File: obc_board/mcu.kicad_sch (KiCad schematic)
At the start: 47 parts, among them J4 Micro_SD_Card, U24 TLE9250X, U25 STM32L552ZET6Q, U26 IS66WVH16M8DBLL-100B1LI, Y2 16MHz, Y3 32.768kHz

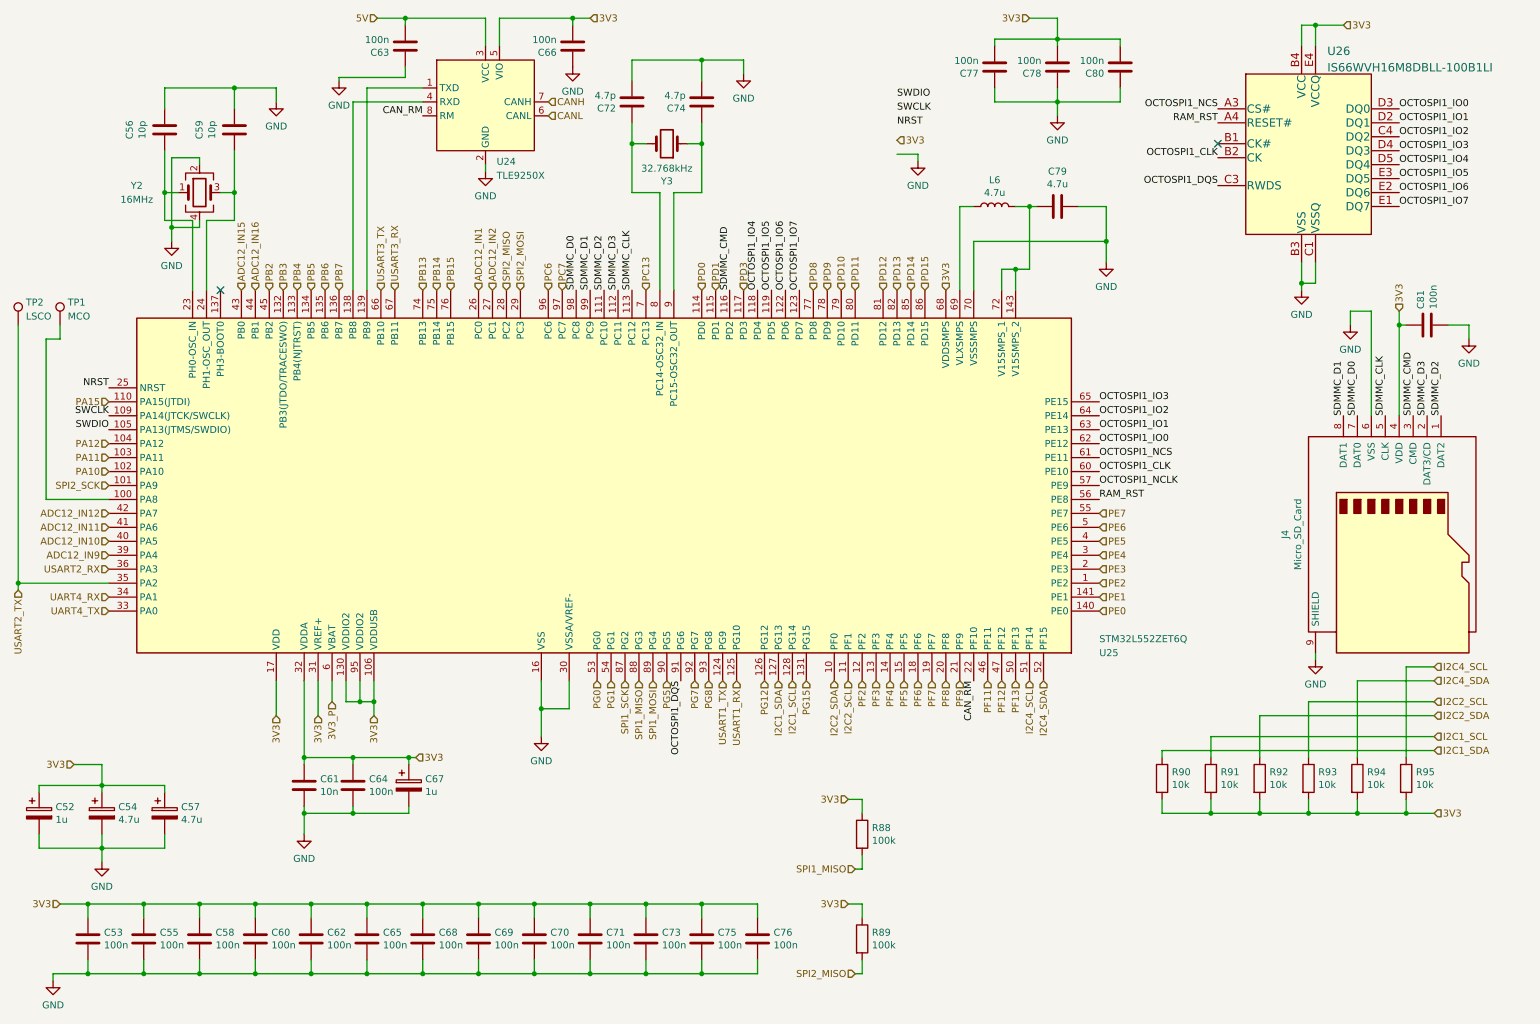
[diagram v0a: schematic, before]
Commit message: remapped magnetorquer pins, routed tespoints
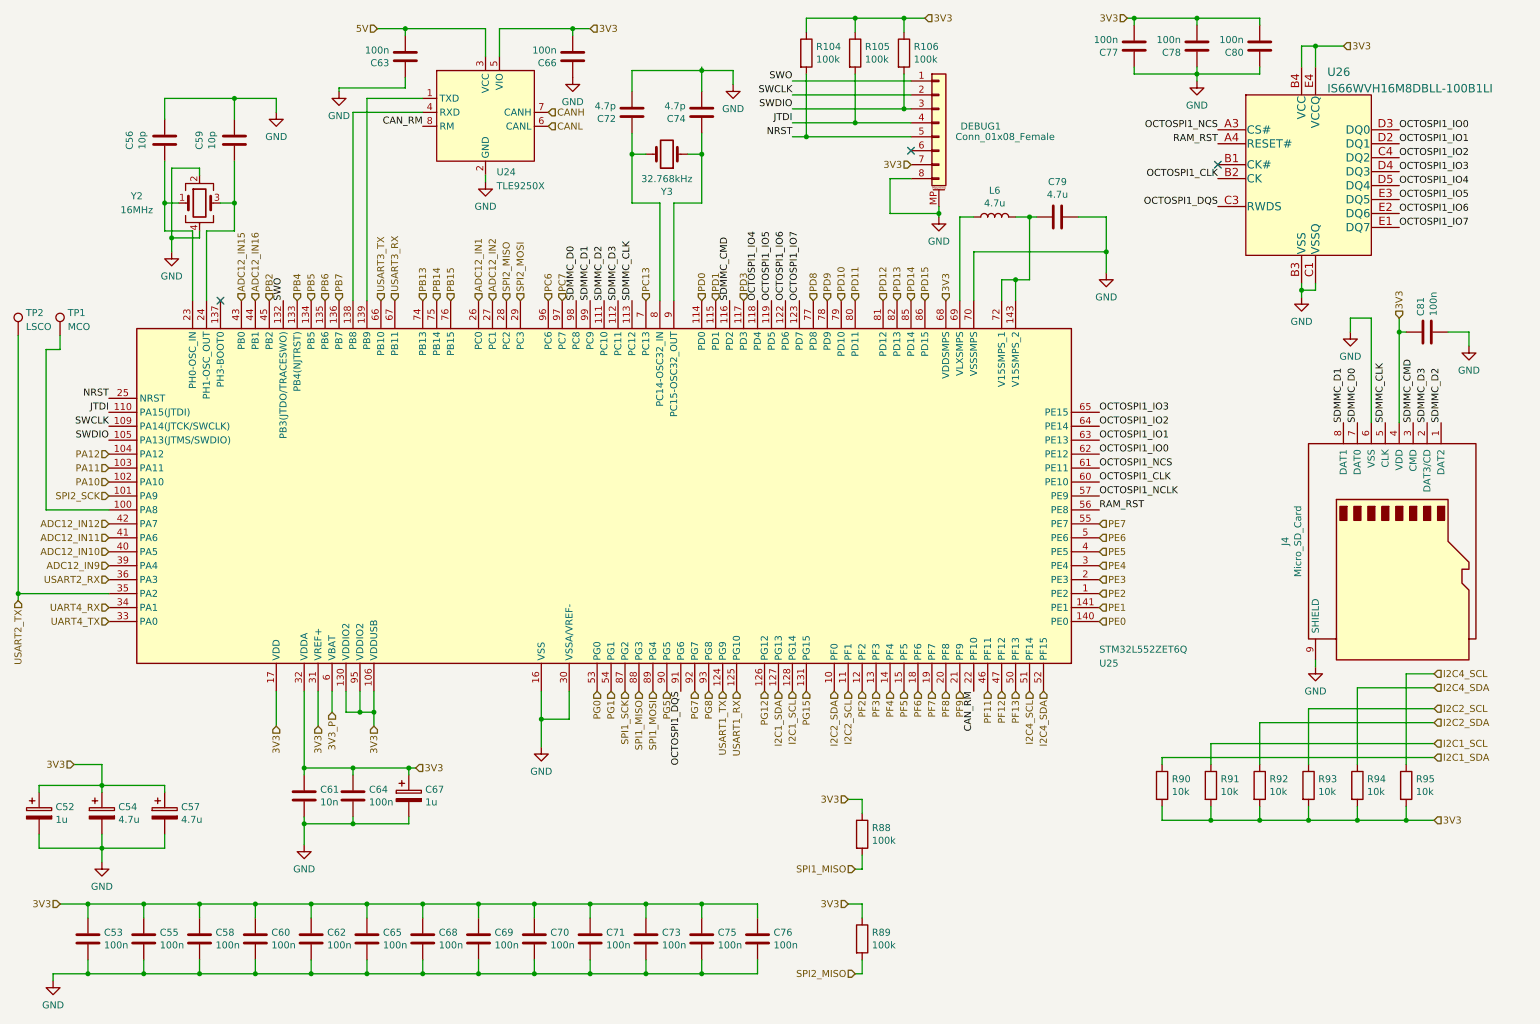
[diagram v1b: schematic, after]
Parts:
- added DEBUG1: Conn_01x08_Female, Connector_Molex:Molex_PicoBlade_53261-0871_1x08-1MP_P1.25mm_Horizontal, symbol Connector_Generic_MountingPin:Conn_01x08_MountingPin
- added R104, R105, R106: 100k, Resistor_SMD:R_0402_1005Metric, symbol Device:R
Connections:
- net GND: now also DEBUG1.8 (Pin_8), DEBUG1.MP (MountPin)
- net NRST: now also DEBUG1.5 (Pin_5), R104.2
- net SWCLK: now also DEBUG1.2 (Pin_2)
- net SWDIO: now also DEBUG1.3 (Pin_3), R106.2
- net VCCQ: now also DEBUG1.7 (Pin_7), R104.1, R105.1, R106.1
- net PA15 renamed JTDI
- net JTDI: now also DEBUG1.4 (Pin_4), R105.2
- net PB3 renamed SWO
- net SWO: now also DEBUG1.1 (Pin_1)
- no-connect marks 2 -> 3
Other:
- moved on the sheet: C56, C59, C61, C63, C64, C66, C67, C72, C74, C77, C78, C79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

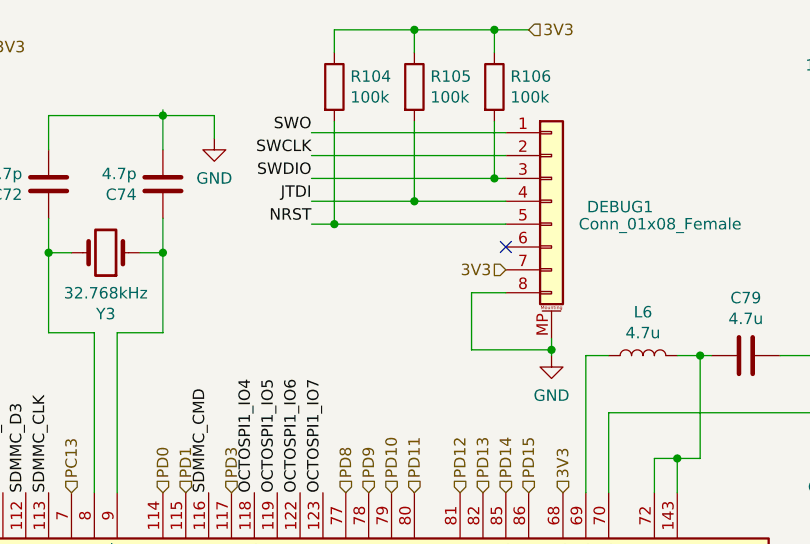
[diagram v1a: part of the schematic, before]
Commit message: routed photodiode circuits, jtag and short circuit prot circuits
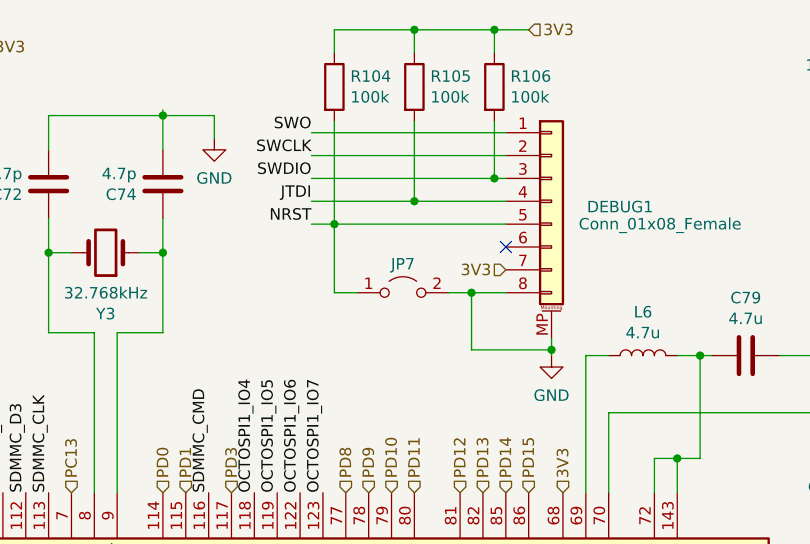
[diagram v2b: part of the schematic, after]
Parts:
- added JP7: Jumper_2_Open, Jumper:SolderJumper-2_P1.3mm_Open_RoundedPad1.0x1.5mm, symbol Jumper:Jumper_2_Open
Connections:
- net GND: now also JP7.2 (B)
- net NRST: now also JP7.1 (A)
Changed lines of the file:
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@@
   (junction (at 166.37 15.24) (diameter 0) (color 0 0 0 0)
+  )
+  (junction (at 172.72 44.45) (diameter 0) (color 0 0 0 0)
   )
   (junction (at 57.15 189.23) (diameter 0) (color 0 0 0 0)
@@
     (stroke (width 0) (type default) (color 0 0 0 0))
   )
+  (wire (pts (xy 170.18 44.45) (xy 172.72 44.45))
+    (stroke (width 0) (type default) (color 0 0 0 0))
+  )
   (wire (pts (xy 78.74 141.605) (xy 78.74 137.795))
     (stroke (width 0) (type default) (color 0 0 0 0))
@@
     (stroke (width 0) (type default) (color 0 0 0 0))
   )
+  (wire (pts (xy 157.48 44.45) (xy 157.48 36.83))
+    (stroke (width 0) (type default) (color 0 0 0 0))
+  )
   (wire (pts (xy 17.78 154.94) (xy 29.21 154.94))
     (stroke (width 0) (type default) (color 0 0 0 0))
@@
   )
   (wire (pts (xy 114.935 17.145) (xy 114.935 18.415))
+    (stroke (width 0) (type default) (color 0 0 0 0))
+  )
+  (wire (pts (xy 160.02 44.45) (xy 157.48 44.45))
     (stroke (width 0) (type default) (color 0 0 0 0))
   )
@@
     (pin "1")
   )
+  (symbol (lib_id "Jumper:Jumper_2_Open") (at 165.1 44.45 0) (unit 1)
+    (in_bom yes) (on_board yes)
+    (property "Reference" "JP7" (id 0) (at 165.1 41.275 0))
+    (property "Value" "Jumper_2_Open" (id 1) (at 165.1 40.005 0)
+      (effects (font (size 1.27 1.27)) hide)
+    )
+    (property "Footprint" "Jumper:SolderJumper-2_P1.3mm_Open_RoundedPad1.0x1.5mm" (id 2) (at 165.1 44.45 0)
+      (effects (font (size 1.27 1.27)) hide)
+    )
+    (property "Datasheet" "~" (id 3) (at 165.1 44.45 0)
+      (effects (font (size 1.27 1.27)) hide)
+    )
+    (pin "1")
+    (pin "2")
+  )
   (symbol (lib_id "power:GND") (at 109.22 147.955 0) (unit 1)
